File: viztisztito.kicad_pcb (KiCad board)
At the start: 2 copper layers, 149 parts, among them J1 +5V, J2 +3.3V, J3 GND, J4 CURR_DIRECT, J5 CURR_FILT, J6 Micro_SD_Card_Det, J7 USB_OTG, Q1 BS250, Q2 BC850, SW1 SW_ON-OFF, SW2 SW_RESET, U1 VTX-214-020-115, U10 MAX803, U2 RT7297BHZSP, U3 RT7297BHZSP, U4 TLP293-4, U5 ACS722, U6 MCP3004, U7 TC77, U8 SN74AHC1G125DBVR, U9 FT230XQ

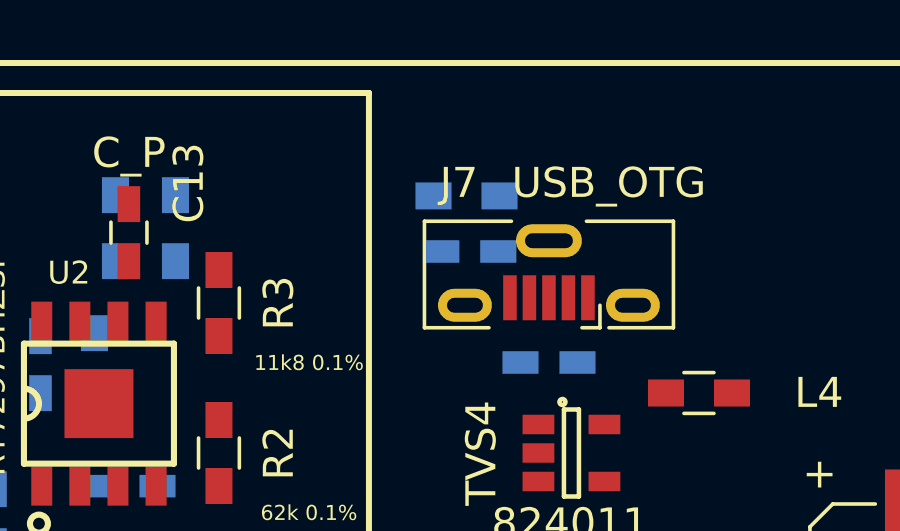
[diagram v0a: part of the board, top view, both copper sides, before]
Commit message: back label positions corrected
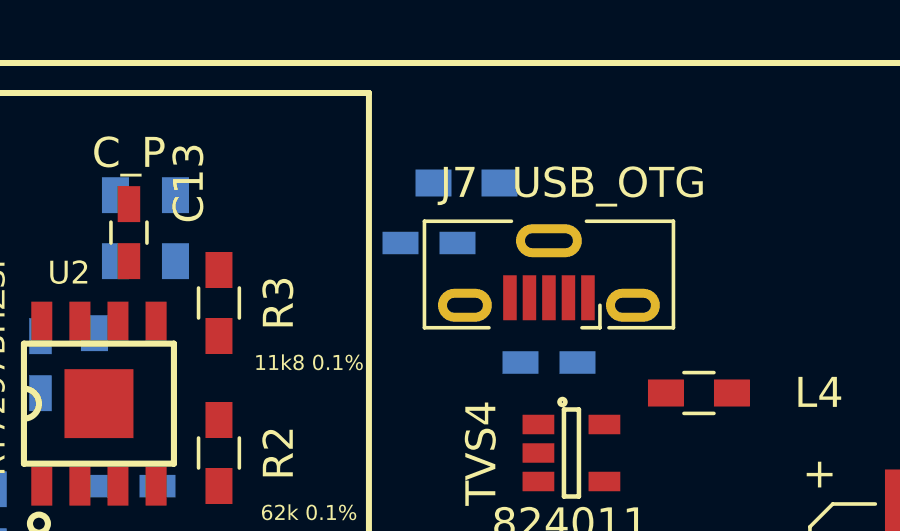
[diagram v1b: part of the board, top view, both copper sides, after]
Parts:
- FL3: value EMI_Filter_CommonMode -> EMI_Filter
- moved C39 1.39 mm to (109.0, 43.0)
- moved R21 0.43 mm to (110.3, 41.0)

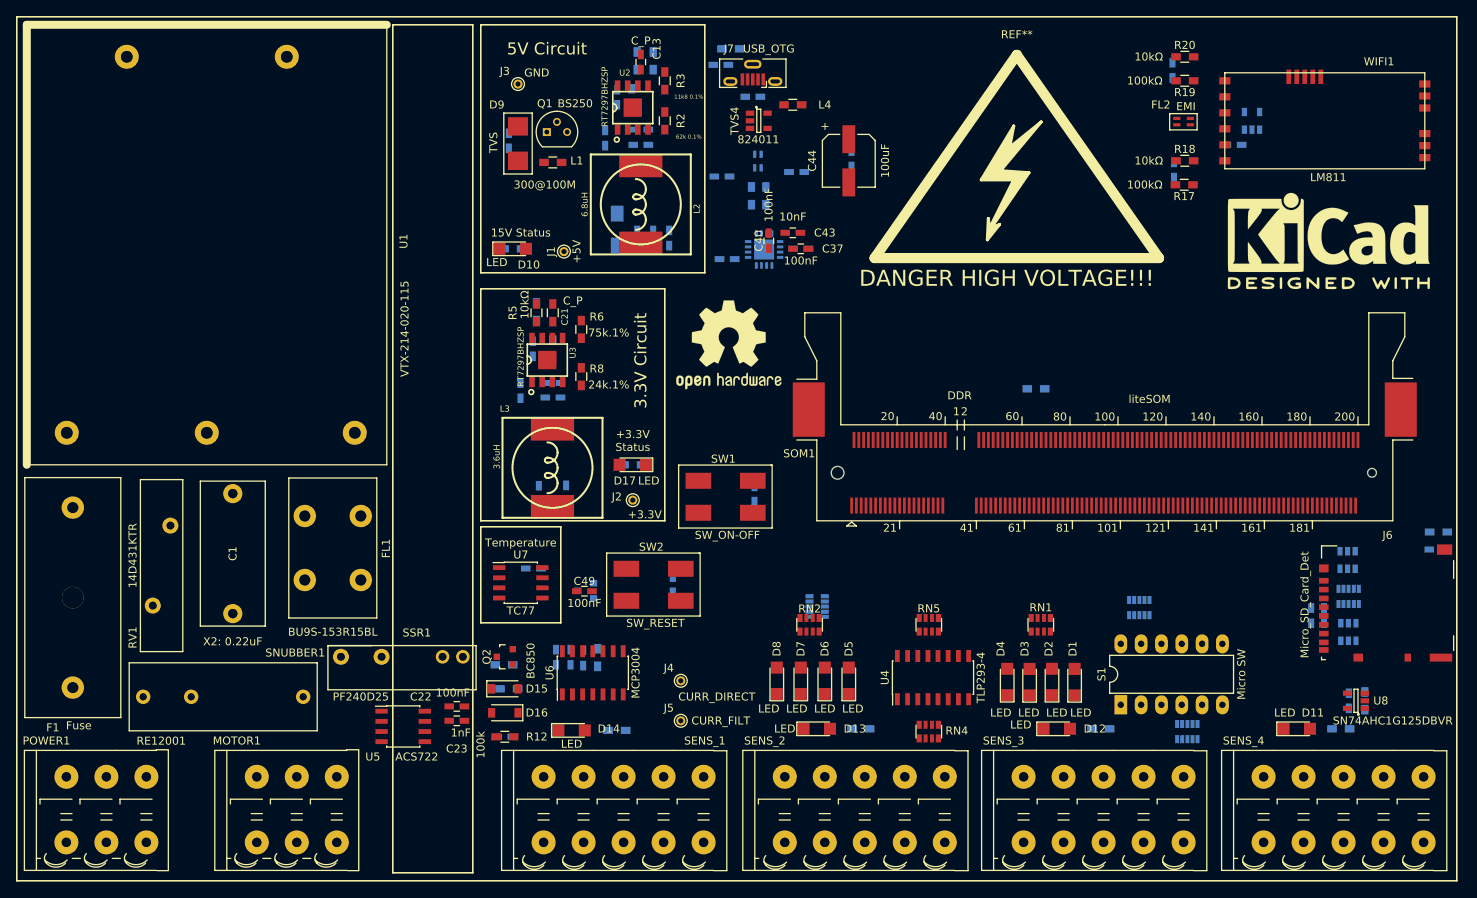
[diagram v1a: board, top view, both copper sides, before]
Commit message: back-front positions and labels verified
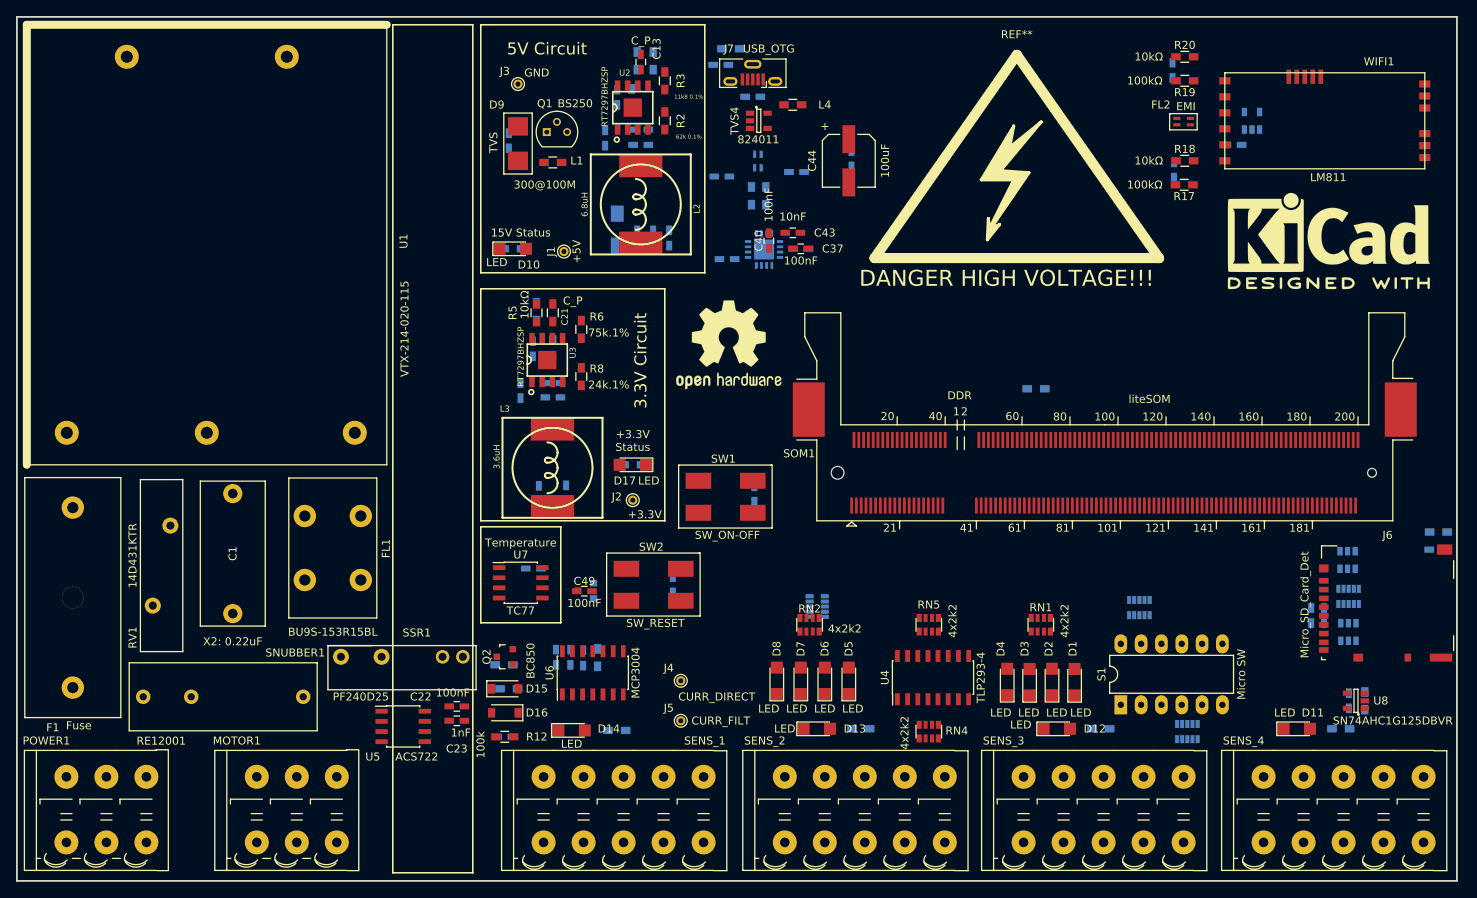
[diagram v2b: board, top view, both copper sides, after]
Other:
- board outline added: 180 x 108 mm

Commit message: almost completely routed; few missing routes
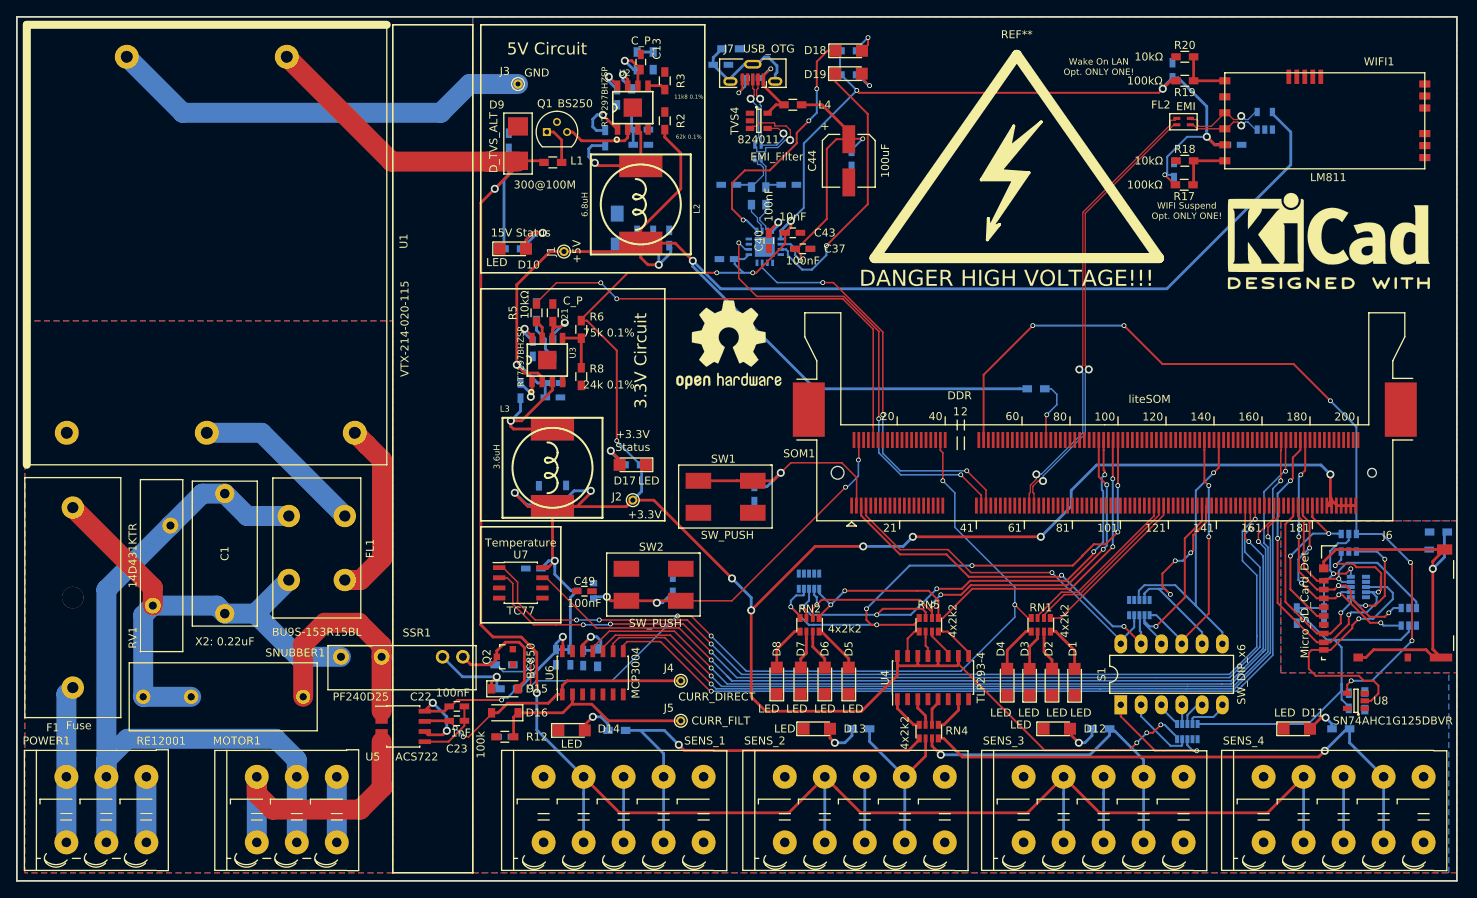
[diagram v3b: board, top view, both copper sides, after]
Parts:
- added D18: TX, LEDs:LED_1206, F.Cu at (125.0, 44.1)
- added D19: RX, LEDs:LED_1206, F.Cu at (125.0, 41.2)
- added R29: 2kΩ, Resistors_SMD:R_0603_HandSoldering, B.Cu at (125.0, 44.2)
- added R30: 2kΩ, Resistors_SMD:R_0603_HandSoldering, B.Cu at (125.0, 41.2)
- D9: value TVS -> D_TVS_ALT
- R6: value 75k.1% -> 75k 0.1%
- R8: value 24k.1% -> 24k 0.1%
- S1: value Micro SW -> SW_DIP_x6
- SW1: value SW_ON-OFF -> SW_PUSH
- SW2: value SW_RESET -> SW_PUSH
- moved TVS2 7.79 mm to (195.0, 112.0)
- moved C46 2.33 mm to (113.0, 44.7)
- moved TVS1 2.16 mm to (187.5, 102.8)
- moved FL1 2.00 mm to (55.0, 107.4)
- moved C42 1.87 mm to (117.5, 58.0)
- moved RN7 1.81 mm to (187.8, 107.0), turned to 270 degrees
- moved C30 1.80 mm to (181.0, 111.8)
- moved RN6 1.65 mm to (118.8, 108.5), turned to 0 degrees
- moved TVS3 1.60 mm to (177.0, 50.0)
- moved C41 1.35 mm to (110.0, 58.0)
- moved FL3 1.14 mm to (113.2, 54.8)
- moved C1 1.00 mm to (47.0, 111.6)
- moved U9 0.35 mm to (114.5, 65.8)
- moved C36 0.25 mm to (119.2, 66.0)
- moved C37 0.25 mm to (119.2, 66.0)
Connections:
- net /system_on_module/Serial Debug/DLNEG renamed /system_on_module/Serial Debug/DL-
- net /system_on_module/Serial Debug/DLPOS renamed /system_on_module/Serial Debug/DL+
- net Net-(R22-Pad2) renamed /system_on_module/Serial Debug/SER_USB-
- net Net-(R23-Pad2) renamed /system_on_module/Serial Debug/SER_USB+
- U9 pad 2: Net-(U9-Pad2) -> /system_on_module/DBG_TXD
- U9 pad 5: (no net) -> Net-(D19-Pad1)
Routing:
- net +3.3V: track 0.00 -> 507.4 mm, vias 0 -> 26
- net +15V: track 0.00 -> 273.0 mm, vias 0 -> 2
- net +5V: track 0.00 -> 249.4 mm, vias 0 -> 3
- net /T_SIO: track 0.00 -> 122.3 mm, vias 0 -> 4
- net /T_SCK: track 0.00 -> 122.2 mm, vias 0 -> 4
- net /T_CS: track 0.00 -> 117.2 mm, vias 0 -> 2
- net /AD_MISO: track 0.00 -> 116.6 mm, vias 0 -> 2
- net /AD_CS: track 0.00 -> 113.9 mm, vias 0 -> 2
- net /AD_CLK: track 0.00 -> 109.4 mm, vias 0 -> 2
- net /SSR_ON: track 0.00 -> 107.6 mm, vias 0 -> 6
- net /AD_MOSI: track 0.00 -> 107.0 mm, vias 0 -> 2
- net /system_on_module/SD1_CARDDETECT: track 0.00 -> 105.5 mm, vias 0 -> 6
- net 230V_NEUTRAL: track 0.00 -> 98.9 mm
- net /DWL0: track 0.00 -> 72.6 mm, vias 0 -> 6
- net Net-(R25-Pad1): track 0.00 -> 69.8 mm, vias 0 -> 1
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- added copper zone on B.Cu, net 230V_GND
- added copper zone on F.Cu, net 230V_GND
- added copper zone on B.Cu, net GND
- added copper zone on F.Cu, net GND
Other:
- net class 0.4 added: clearance 0.3, trace_width 0.35, via_dia 1, via_drill 0.6
- net class 2 added: clearance 2, trace_width 2.5, via_dia 6, via_drill 4
- net class thin added: clearance 0.1, trace_width 0.2, via_dia 0.6, via_drill 0.4
- board text added: "WIFI Suspend Opt. ONLY ONE!"
- board text added: "Wake On LAN Opt. ONLY ONE!"

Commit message: raw routing finished
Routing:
- net GND: track 65.9 -> 321.9 mm, vias 1 -> 18
- net +5V: track 249.4 -> 429.9 mm, vias 3 -> 5
- net +3.3V: track 507.4 -> 510.0 mm, vias 26 -> 27
- net Net-(D15-Pad2): track 15.6 -> 17.3 mm
- net /SSR_ON: track 107.6 -> 109.2 mm, vias 6 -> 8

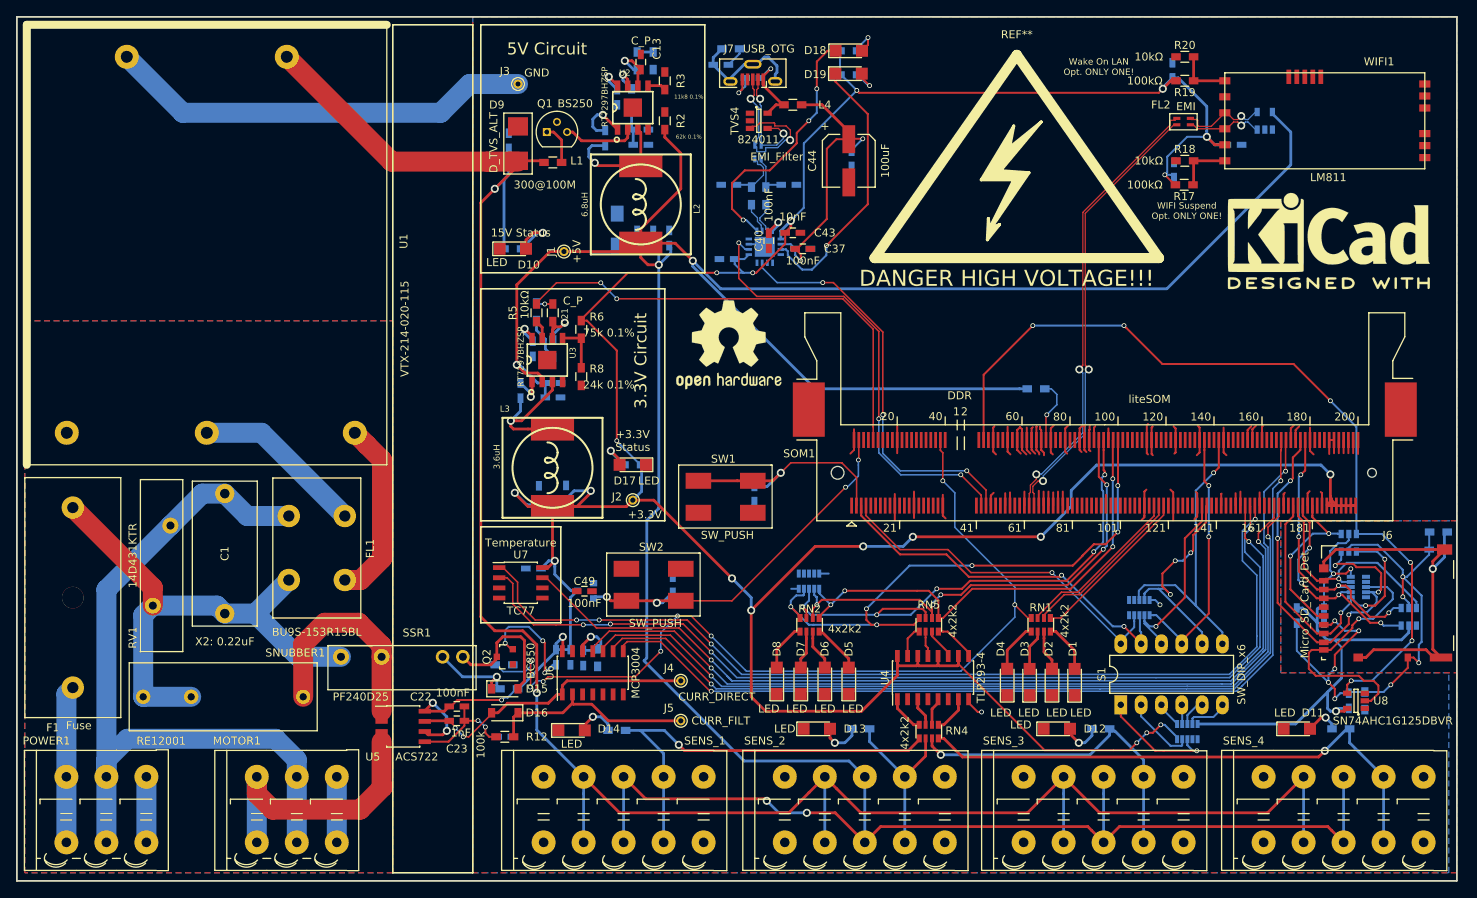
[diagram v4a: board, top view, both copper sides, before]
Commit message: fully routed
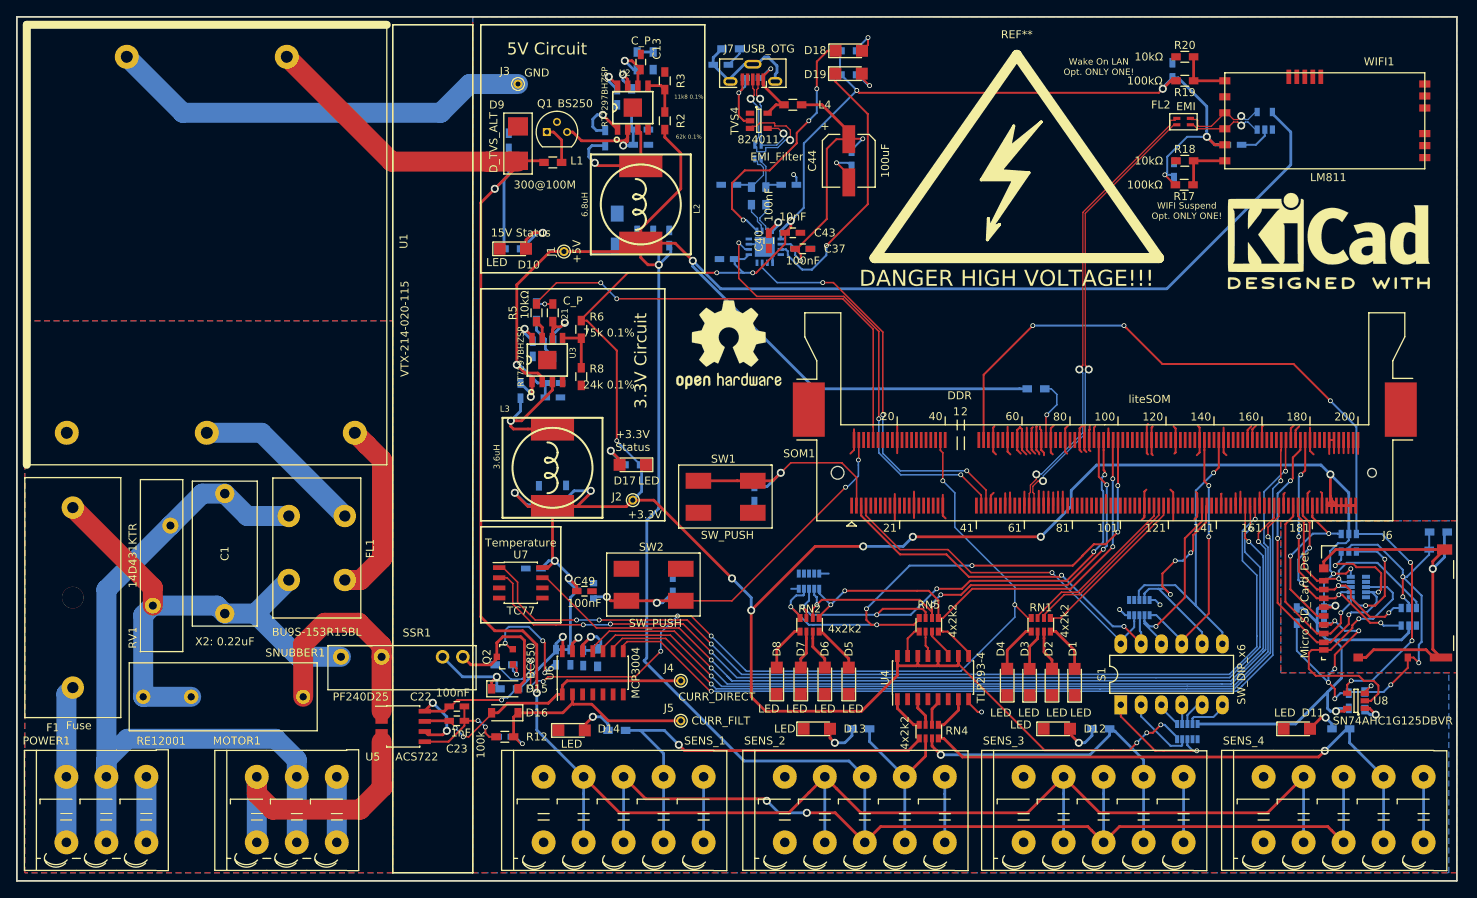
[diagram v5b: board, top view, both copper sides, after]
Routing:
- net GND: track 321.9 -> 344.0 mm, vias 18 -> 22
- net +3.3V: track 510.0 -> 527.0 mm, vias 27 -> 30
- net Net-(SENS_4-Pad5): track 0.00 -> 8.20 mm
- net Net-(SENS_3-Pad5): track 0.00 -> 8.20 mm
- net Net-(SENS_2-Pad5): track 0.00 -> 8.20 mm
- net Net-(SENS_1-Pad5): track 0.00 -> 8.20 mm
- net Net-(C3-Pad1): track 14.1 -> 17.6 mm, vias 0 -> 1
- net Net-(R16-Pad1): track 0.00 -> 3.32 mm, vias 0 -> 1
- net /DIGITAL_COMM/ADCH1: track 26.1 -> 29.1 mm, vias 0 -> 1
- net Net-(Q2-Pad1): track 0.00 -> 2.82 mm, vias 0 -> 1
- net Net-(R2-Pad2): track 2.30 -> 5.10 mm
- net /SSR_ON: track 109.2 -> 110.3 mm
